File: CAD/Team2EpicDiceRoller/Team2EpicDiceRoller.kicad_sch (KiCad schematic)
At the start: 77 parts, among them J1 Conn_02x03_Odd_Even, J2 Conn_01x16, J3 Barrel_Jack, Q1 BSS138, SW1 SW_Toggle_SPDT, SW2 Tilt_Switch, SW3 SW_Power, SW4 RotaryEncoder_Switch, SW5 SW_LeftMenu, SW6 SW_MidMenu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

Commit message: Revert "Updated the IO again"
This reverts commit 80c1a5cda0b79e003991432f29007fe40f1553a5.
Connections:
- net AD0_PC0: no longer U2.2
- net IO10_SS_PB2: now also U2.6
- net IO5_PD5: now also U2.2; no longer U2.4
- net IO6_PD6: now also U2.4; no longer U2.6
- net LeftDebn: now also U2.1; no longer U2.3
- net MidDebn: now also U2.3; no longer U2.5
- net RigDebn: now also U2.5; no longer U2.1
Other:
- moved on the sheet: U2A, U2B, U2C
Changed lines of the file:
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@@
+    (stroke (width 0) (type default) (color 0 0 0 0))
+  )
+  (wire (pts (xy 270.51 30.48) (xy 276.86 30.48))
     (stroke (width 0) (type default) (color 0 0 0 0))
   )
@@
     )
   )
-  (global_label "AD0_PC0" (shape input) (at 270.51 30.48 0) (fields_autoplaced)
+  (global_label "IO10_SS_PB2" (shape input) (at 276.86 30.48 90) (fields_autoplaced)
     (effects (font (size 1.27 1.27)) (justify left))
-    (property "Intersheet References" "${INTERSHEET_REFS}" (id 0) (at 281.2083 30.5594 0)
+    (property "Intersheet References" "${INTERSHEET_REFS}" (id 0) (at 276.9394 15.6088 90)
       (effects (font (size 1.27 1.27)) (justify left) hide)
     )
@@
     (pin "9")
   )
-  (symbol (lib_id "74xx:74HC14") (at 143.51 30.48 0) (unit 2)
+  (symbol (lib_id "74xx:74HC14") (at 143.51 30.48 0) (unit 1)
     (in_bom yes) (on_board yes) (fields_autoplaced)
     (property "Reference" "U2" (id 0) (at 143.51 21.59 0))
@@
       (effects (font (size 1.27 1.27)) hide)
     )
-    (pin "3")
-    (pin "4")
+    (pin "1")
+    (pin "2")
   )
   (symbol (lib_id "74xx:74HC14") (at 143.51 54.61 0) (unit 5)
@@
     (pin "13")
   )
-  (symbol (lib_id "74xx:74HC14") (at 203.2 30.48 0) (unit 3)
+  (symbol (lib_id "74xx:74HC14") (at 203.2 30.48 0) (unit 2)
     (in_bom yes) (on_board yes) (fields_autoplaced)
     (property "Reference" "U2" (id 0) (at 203.2 21.59 0))
@@
       (effects (font (size 1.27 1.27)) hide)
     )
-    (pin "5")
-    (pin "6")
-  )
-  (symbol (lib_id "74xx:74HC14") (at 262.89 30.48 0) (unit 1)
+    (pin "3")
+    (pin "4")
+  )
+  (symbol (lib_id "74xx:74HC14") (at 262.89 30.48 0) (unit 3)
     (in_bom yes) (on_board yes) (fields_autoplaced)
     (property "Reference" "U2" (id 0) (at 262.89 21.59 0))
@@
       (effects (font (size 1.27 1.27)) hide)
     )
-    (pin "1")
-    (pin "2")
+    (pin "5")
+    (pin "6")
   )
   (symbol (lib_name "RotaryEncoder_Switch_1") (lib_id "Device:RotaryEncoder_Switch") (at 36.83 33.02 0) (unit 1)

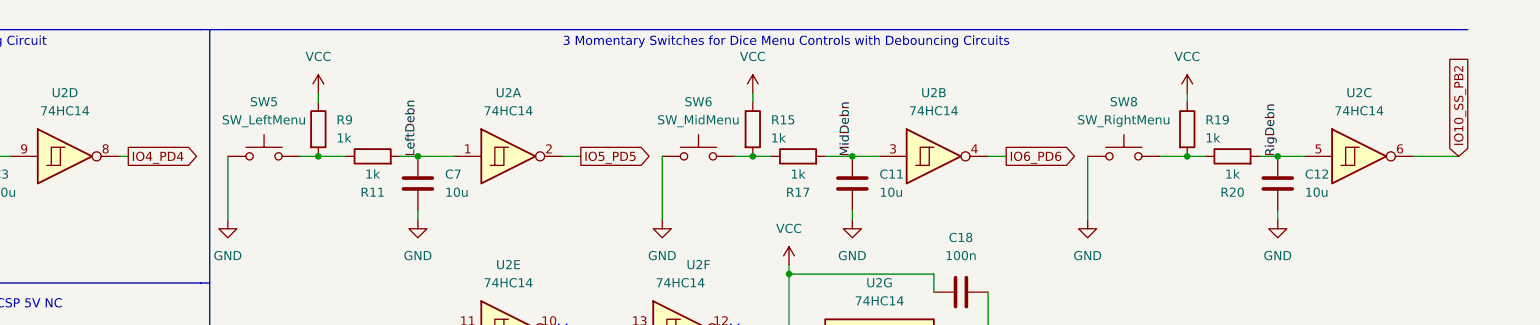
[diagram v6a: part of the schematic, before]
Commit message: minor changes to text
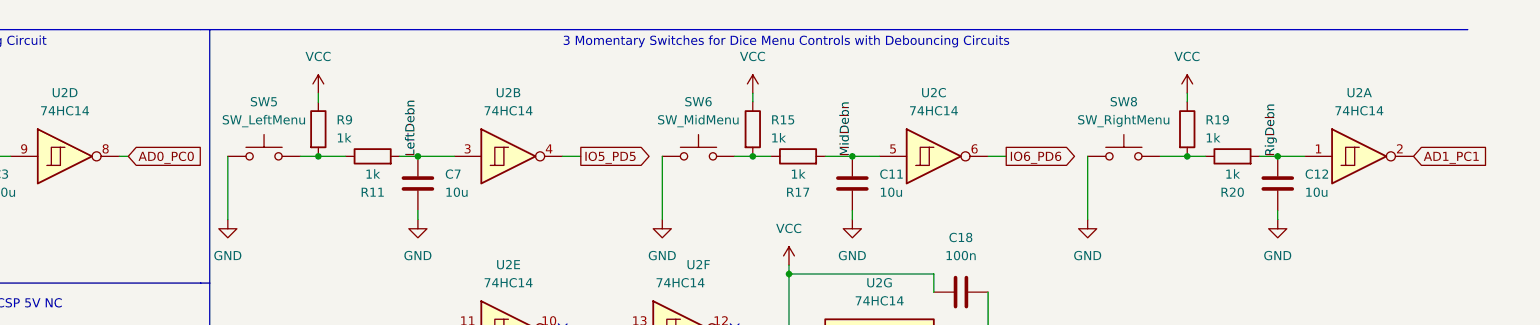
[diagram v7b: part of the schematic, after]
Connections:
- net AD0_PC0: now also U2.8
- net AD1_PC1: now also U2.2
- net IO10_SS_PB2: no longer U2.6
- net IO4_PD4: no longer U2.8
- net IO5_PD5: now also U2.4; no longer U2.2
- net IO6_PD6: now also U2.6; no longer U2.4
- net LeftDebn: now also U2.3; no longer U2.1
- net MidDebn: now also U2.5; no longer U2.3
- net RigDebn: now also U2.1; no longer U2.5
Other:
- title: Team 2 - Dice Roller Schematic -> Team 2 - Epic Dice Roller Schematic
- moved on the sheet: U2A, U2B, U2C
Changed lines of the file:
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@@
   (paper "A4")
   (title_block
-    (title "Team 2 - Dice Roller Schematic")
-    (date "2021-10-27")
+    (title "Team 2 - Epic Dice Roller Schematic")
+    (date "2021-11-17")
     (rev "1")
     (comment 1 "Braden Harwood, Stephen Short")
     (comment 2 "Drew Seidel, Michael Weston")
+    (comment 3 "Portland State University")
   )
   (junction (at 31.75 156.21) (diameter 0) (color 0 0 0 0))
@@
     (stroke (width 0) (type default) (color 0 0 0 0))
   )
-  (wire (pts (xy 270.51 30.48) (xy 276.86 30.48))
-    (stroke (width 0) (type default) (color 0 0 0 0))
-  )
   (wire (pts (xy 275.59 77.47) (xy 275.59 80.01))
     (stroke (width 0) (type default) (color 0 0 0 0))
@@
     )
   )
-  (global_label "IO4_PD4" (shape output) (at 90.17 30.48 0) (fields_autoplaced)
+  (global_label "AD0_PC0" (shape input) (at 90.17 30.48 0) (fields_autoplaced)
     (effects (font (size 1.27 1.27)) (justify left))
-    (property "Intersheet References" "${INTERSHEET_REFS}" (id 0) (at 100.445 30.4006 0)
+    (property "Intersheet References" "${INTERSHEET_REFS}" (id 0) (at 100.8683 30.5594 0)
       (effects (font (size 1.27 1.27)) (justify left) hide)
     )
@@
     )
   )
-  (global_label "IO10_SS_PB2" (shape input) (at 276.86 30.48 90) (fields_autoplaced)
+  (global_label "AD1_PC1" (shape input) (at 270.51 30.48 0) (fields_autoplaced)
     (effects (font (size 1.27 1.27)) (justify left))
-    (property "Intersheet References" "${INTERSHEET_REFS}" (id 0) (at 276.9394 15.6088 90)
+    (property "Intersheet References" "${INTERSHEET_REFS}" (id 0) (at 281.2083 30.5594 0)
       (effects (font (size 1.27 1.27)) (justify left) hide)
     )
@@
     (pin "9")
   )
-  (symbol (lib_id "74xx:74HC14") (at 143.51 30.48 0) (unit 1)
+  (symbol (lib_id "74xx:74HC14") (at 143.51 30.48 0) (unit 2)
     (in_bom yes) (on_board yes) (fields_autoplaced)
     (property "Reference" "U2" (id 0) (at 143.51 21.59 0))
@@
       (effects (font (size 1.27 1.27)) hide)
     )
-    (pin "1")
-    (pin "2")
+    (pin "3")
+    (pin "4")
   )
   (symbol (lib_id "74xx:74HC14") (at 143.51 54.61 0) (unit 5)
@@
     (pin "13")
   )
-  (symbol (lib_id "74xx:74HC14") (at 203.2 30.48 0) (unit 2)
+  (symbol (lib_id "74xx:74HC14") (at 203.2 30.48 0) (unit 3)
     (in_bom yes) (on_board yes) (fields_autoplaced)
     (property "Reference" "U2" (id 0) (at 203.2 21.59 0))
@@
       (effects (font (size 1.27 1.27)) hide)
     )
-    (pin "3")
-    (pin "4")
+    (pin "5")
+    (pin "6")
   )
-  (symbol (lib_id "74xx:74HC14") (at 262.89 30.48 0) (unit 3)
+  (symbol (lib_id "74xx:74HC14") (at 262.89 30.48 0) (unit 1)
     (in_bom yes) (on_board yes) (fields_autoplaced)
     (property "Reference" "U2" (id 0) (at 262.89 21.59 0))
@@
       (effects (font (size 1.27 1.27)) hide)
     )
-    (pin "5")
-    (pin "6")
+    (pin "1")
+    (pin "2")
   )
   (symbol (lib_name "RotaryEncoder_Switch_1") (lib_id "Device:RotaryEncoder_Switch") (at 36.83 33.02 0) (unit 1)

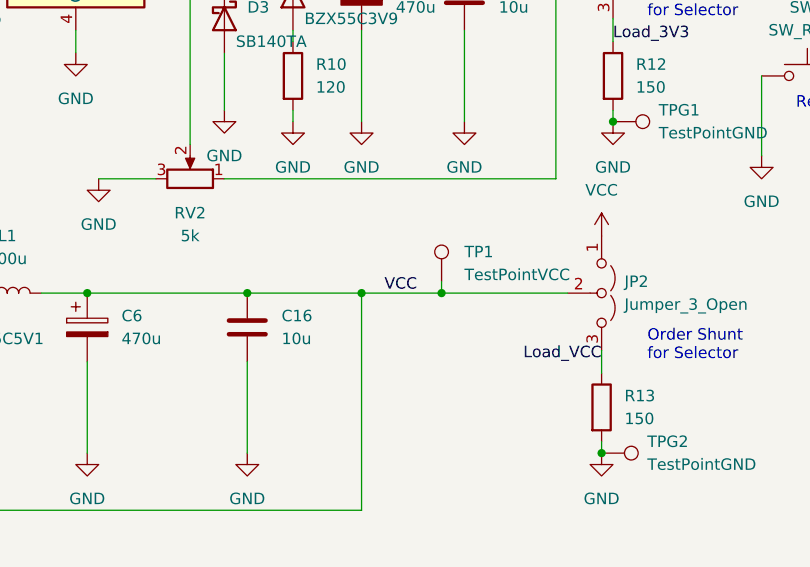
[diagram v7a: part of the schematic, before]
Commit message: Removed extraneous VCC net that caused ghost line between VCC jumper pads
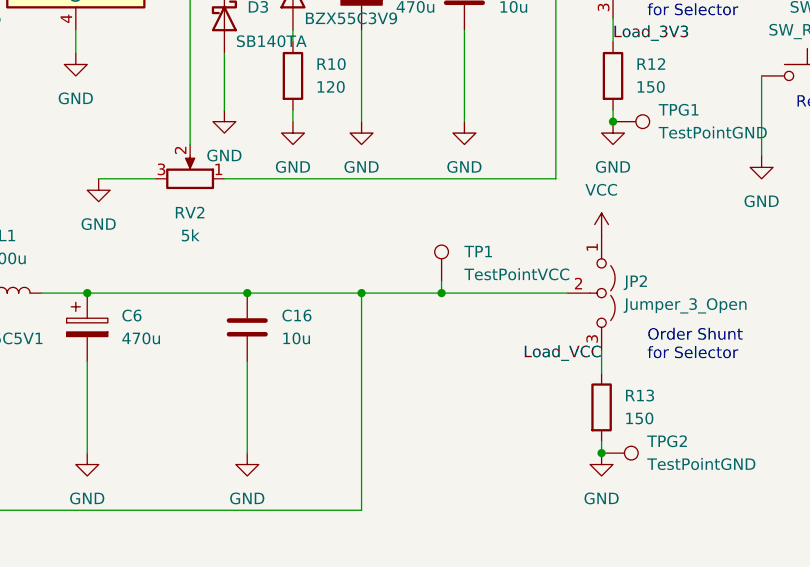
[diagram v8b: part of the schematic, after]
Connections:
- net VCC: no longer C16.1, C6.1, JP2.2 (C), L1.2, RV1.1, TP1.1
- new net: C16.1, C6.1, JP2.2 (C), L1.2, RV1.1, TP1.1
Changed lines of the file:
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@@
-    (effects (font (size 1.27 1.27)) (justify left bottom))
-  )
-  (label "VCC" (at 130.81 166.37 0)
     (effects (font (size 1.27 1.27)) (justify left bottom))
   )
